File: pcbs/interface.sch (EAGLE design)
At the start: 25 parts, among them U1 ISL3179EIBZ, U2 ATMEGA328P

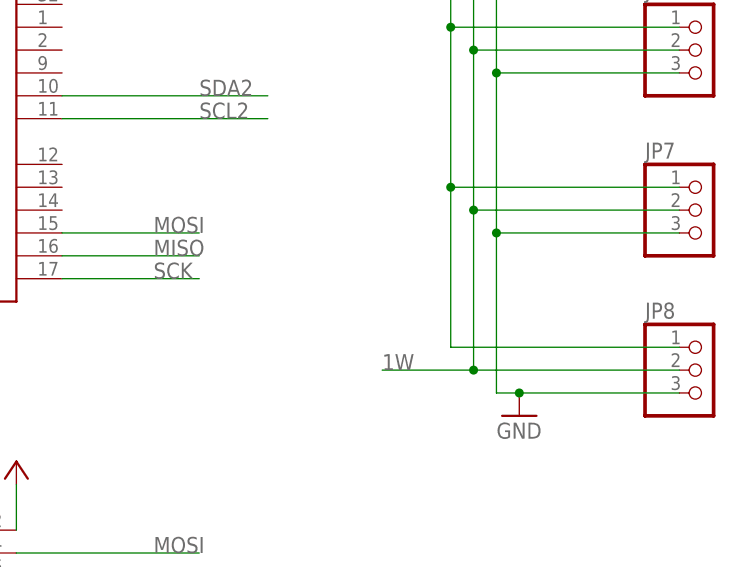
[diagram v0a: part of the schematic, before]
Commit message: added pull up to 1w
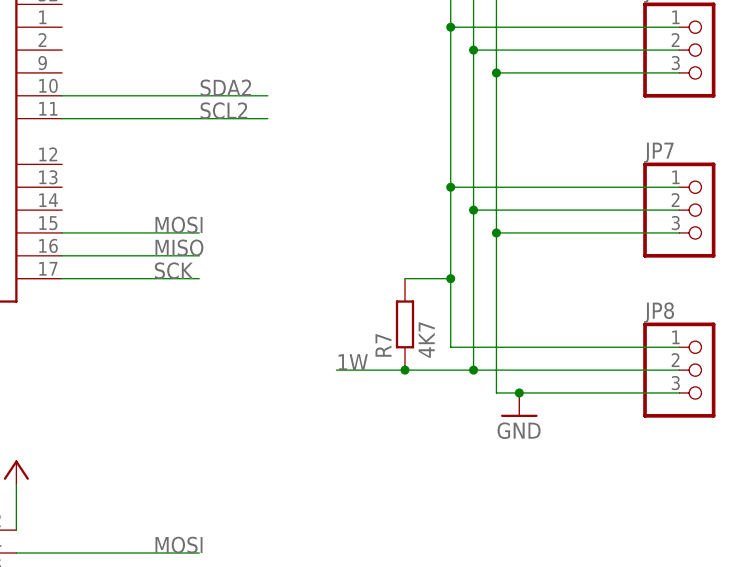
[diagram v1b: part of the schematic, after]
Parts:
- added R7: 4K7, resistor:R-EU_R0805
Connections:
- net 1W: now also R7.1
- net VIN: now also R7.2
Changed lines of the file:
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@@
 <?xml version="1.0" encoding="utf-8"?>
 <!DOCTYPE eagle SYSTEM "eagle.dtd">
-<eagle version="6.6.0">
+<eagle version="6.5.0">
 <drawing>
 <settings>
@@
 <part name="R5" library="resistor" deviceset="R-EU_" device="R0805" value="10k"/>
 <part name="R6" library="resistor" deviceset="R-EU_" device="R0805" value="10k"/>
+<part name="R7" library="resistor" deviceset="R-EU_" device="R0805" value="4K7"/>
 </parts>
 <sheets>
@@
 <instance part="R5" gate="G$1" x="81.28" y="50.8" rot="R90"/>
 <instance part="R6" gate="G$1" x="88.9" y="50.8" rot="R90"/>
+<instance part="R7" gate="G$1" x="208.28" y="68.58" rot="R90"/>
 </instances>
 <busses>
@@
 <wire x1="215.9" y1="81.28" x2="215.9" y2="63.5" width="0.1524" layer="91"/>
 <wire x1="215.9" y1="63.5" x2="238.76" y2="63.5" width="0.1524" layer="91"/>
-<wire x1="215.9" y1="63.5" x2="205.74" y2="63.5" width="0.1524" layer="91"/>
+<wire x1="215.9" y1="63.5" x2="208.28" y2="63.5" width="0.1524" layer="91"/>
 <pinref part="JP6" gate="A" pin="2"/>
+<wire x1="208.28" y1="63.5" x2="200.66" y2="63.5" width="0.1524" layer="91"/>
 <wire x1="238.76" y1="99.06" x2="215.9" y2="99.06" width="0.1524" layer="91"/>
 <pinref part="JP5" gate="A" pin="2"/>
@@
 <junction x="215.9" y="99.06"/>
 <junction x="215.9" y="63.5"/>
-<label x="205.74" y="63.5" size="1.778" layer="95"/>
+<label x="200.66" y="63.5" size="1.778" layer="95"/>
 <pinref part="JP7" gate="A" pin="2"/>
 <wire x1="238.76" y1="81.28" x2="215.9" y2="81.28" width="0.1524" layer="91"/>
 <junction x="215.9" y="81.28"/>
+<pinref part="R7" gate="G$1" pin="1"/>
+<junction x="208.28" y="63.5"/>
 </segment>
 <segment>
@@
 <wire x1="213.36" y1="119.38" x2="213.36" y2="101.6" width="0.1524" layer="91"/>
 <wire x1="213.36" y1="101.6" x2="213.36" y2="83.82" width="0.1524" layer="91"/>
-<wire x1="213.36" y1="83.82" x2="213.36" y2="66.04" width="0.1524" layer="91"/>
+<wire x1="213.36" y1="83.82" x2="213.36" y2="73.66" width="0.1524" layer="91"/>
+<wire x1="213.36" y1="73.66" x2="213.36" y2="66.04" width="0.1524" layer="91"/>
 <wire x1="213.36" y1="66.04" x2="238.76" y2="66.04" width="0.1524" layer="91"/>
 <pinref part="JP5" gate="A" pin="1"/>
@@
 <junction x="213.36" y="83.82"/>
 <label x="213.36" y="137.16" size="1.778" layer="95"/>
-</segment>
-</net>
+<pinref part="R7" gate="G$1" pin="2"/>
+<wire x1="213.36" y1="73.66" x2="208.28" y2="73.66" width="0.1524" layer="91"/>
+<junction x="213.36" y="73.66"/>
+</segment>
+</net>

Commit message: Now has pin for rs485 tx enable
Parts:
- removed R1: 1k, resistor:R-EU_R0805
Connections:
- removed net N$1: R1.1, U1.DE
- new net TXEN: U1.DE, U2.PD2(INT0)
- net VCC: no longer R1.2
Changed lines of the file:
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@@
 <?xml version="1.0" encoding="utf-8"?>
 <!DOCTYPE eagle SYSTEM "eagle.dtd">
-<eagle version="6.5.0">
+<eagle version="6.6.0">
 <drawing>
 <settings>
@@
 <part name="C1" library="resistor" deviceset="CPOL-EU" device="A/3216-18R" value="22uF"/>
 <part name="GND3" library="supply1" deviceset="GND" device=""/>
-<part name="R1" library="resistor" deviceset="R-EU_" device="R0805" value="1k"/>
 <part name="ISP1" library="adafruit" deviceset="AVRISP" device="-6"/>
 <part name="P+2" library="glacsweb" deviceset="VCC" device=""/>
@@
 <instance part="C1" gate="G$1" x="45.72" y="149.86"/>
 <instance part="GND3" gate="1" x="20.32" y="81.28"/>
-<instance part="R1" gate="G$1" x="12.7" y="91.44" rot="R90"/>
 <instance part="ISP1" gate="G$1" x="149.86" y="43.18"/>
 <instance part="P+2" gate="VCC" x="165.1" y="53.34"/>
@@
 <pinref part="U1" gate="A" pin="VCC"/>
 <wire x1="25.4" y1="99.06" x2="12.7" y2="99.06" width="0.1524" layer="91"/>
-<pinref part="R1" gate="G$1" pin="2"/>
-<wire x1="12.7" y1="96.52" x2="12.7" y2="99.06" width="0.1524" layer="91"/>
-<junction x="12.7" y="99.06"/>
 </segment>
 <segment>
@@
 </segment>
 </net>
-<net name="N$1" class="0">
+<net name="TXEN" class="0">
 <segment>
 <pinref part="U1" gate="A" pin="DE"/>
-<wire x1="25.4" y1="91.44" x2="17.78" y2="91.44" width="0.1524" layer="91"/>
-<wire x1="17.78" y1="91.44" x2="17.78" y2="86.36" width="0.1524" layer="91"/>
-<pinref part="R1" gate="G$1" pin="1"/>
-<wire x1="17.78" y1="86.36" x2="12.7" y2="86.36" width="0.1524" layer="91"/>
-</segment>
-</net>
+<wire x1="25.4" y1="91.44" x2="7.62" y2="91.44" width="0.1524" layer="91"/>
+<label x="7.62" y="91.44" size="1.778" layer="95"/>
+</segment>
+<segment>
+<pinref part="U2" gate="G$1" pin="PD2(INT0)"/>
+<wire x1="170.18" y1="104.14" x2="193.04" y2="104.14" width="0.1524" layer="91"/>
+<label x="185.42" y="104.14" size="1.778" layer="95"/>
+</segment>
+</net>

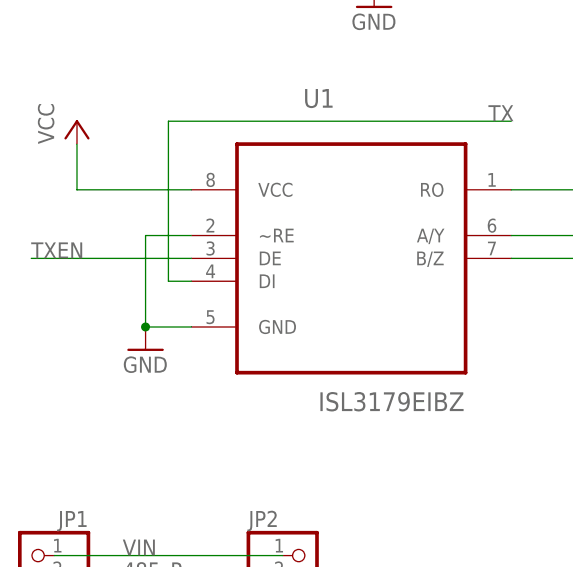
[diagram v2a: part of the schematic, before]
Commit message: now has control of rx as well
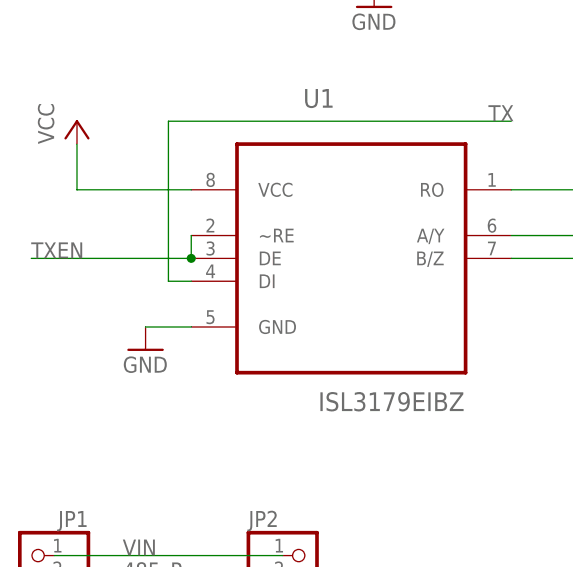
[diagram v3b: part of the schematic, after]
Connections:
- net GND: no longer U1.~RE
- net TXEN: now also U1.~RE
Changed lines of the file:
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@@
 <net name="GND" class="0">
 <segment>
+<pinref part="GND3" gate="1" pin="GND"/>
 <pinref part="U1" gate="A" pin="GND"/>
-<pinref part="GND3" gate="1" pin="GND"/>
 <wire x1="25.4" y1="83.82" x2="20.32" y2="83.82" width="0.1524" layer="91"/>
-<pinref part="U1" gate="A" pin="~RE"/>
-<wire x1="25.4" y1="93.98" x2="20.32" y2="93.98" width="0.1524" layer="91"/>
-<wire x1="20.32" y1="93.98" x2="20.32" y2="83.82" width="0.1524" layer="91"/>
-<junction x="20.32" y="83.82"/>
 </segment>
 <segment>
@@
 <wire x1="25.4" y1="91.44" x2="7.62" y2="91.44" width="0.1524" layer="91"/>
 <label x="7.62" y="91.44" size="1.778" layer="95"/>
+<pinref part="U1" gate="A" pin="~RE"/>
+<wire x1="25.4" y1="93.98" x2="25.4" y2="91.44" width="0.1524" layer="91"/>
+<junction x="25.4" y="91.44"/>
 </segment>
 <segment>
